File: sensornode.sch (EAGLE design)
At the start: 71 parts, among them IC1 CP2104, Q1 mmbt2222, Q2 mmbt2222, Q3 DMG3415U, SW2 KMR2, U1 TSL2591, U2 AP2112-3.3, U3 MCP73831T-2ACI/OT, U4 BMEx80, X2 ESP32_WROOM32_SKINNY, X4 20329

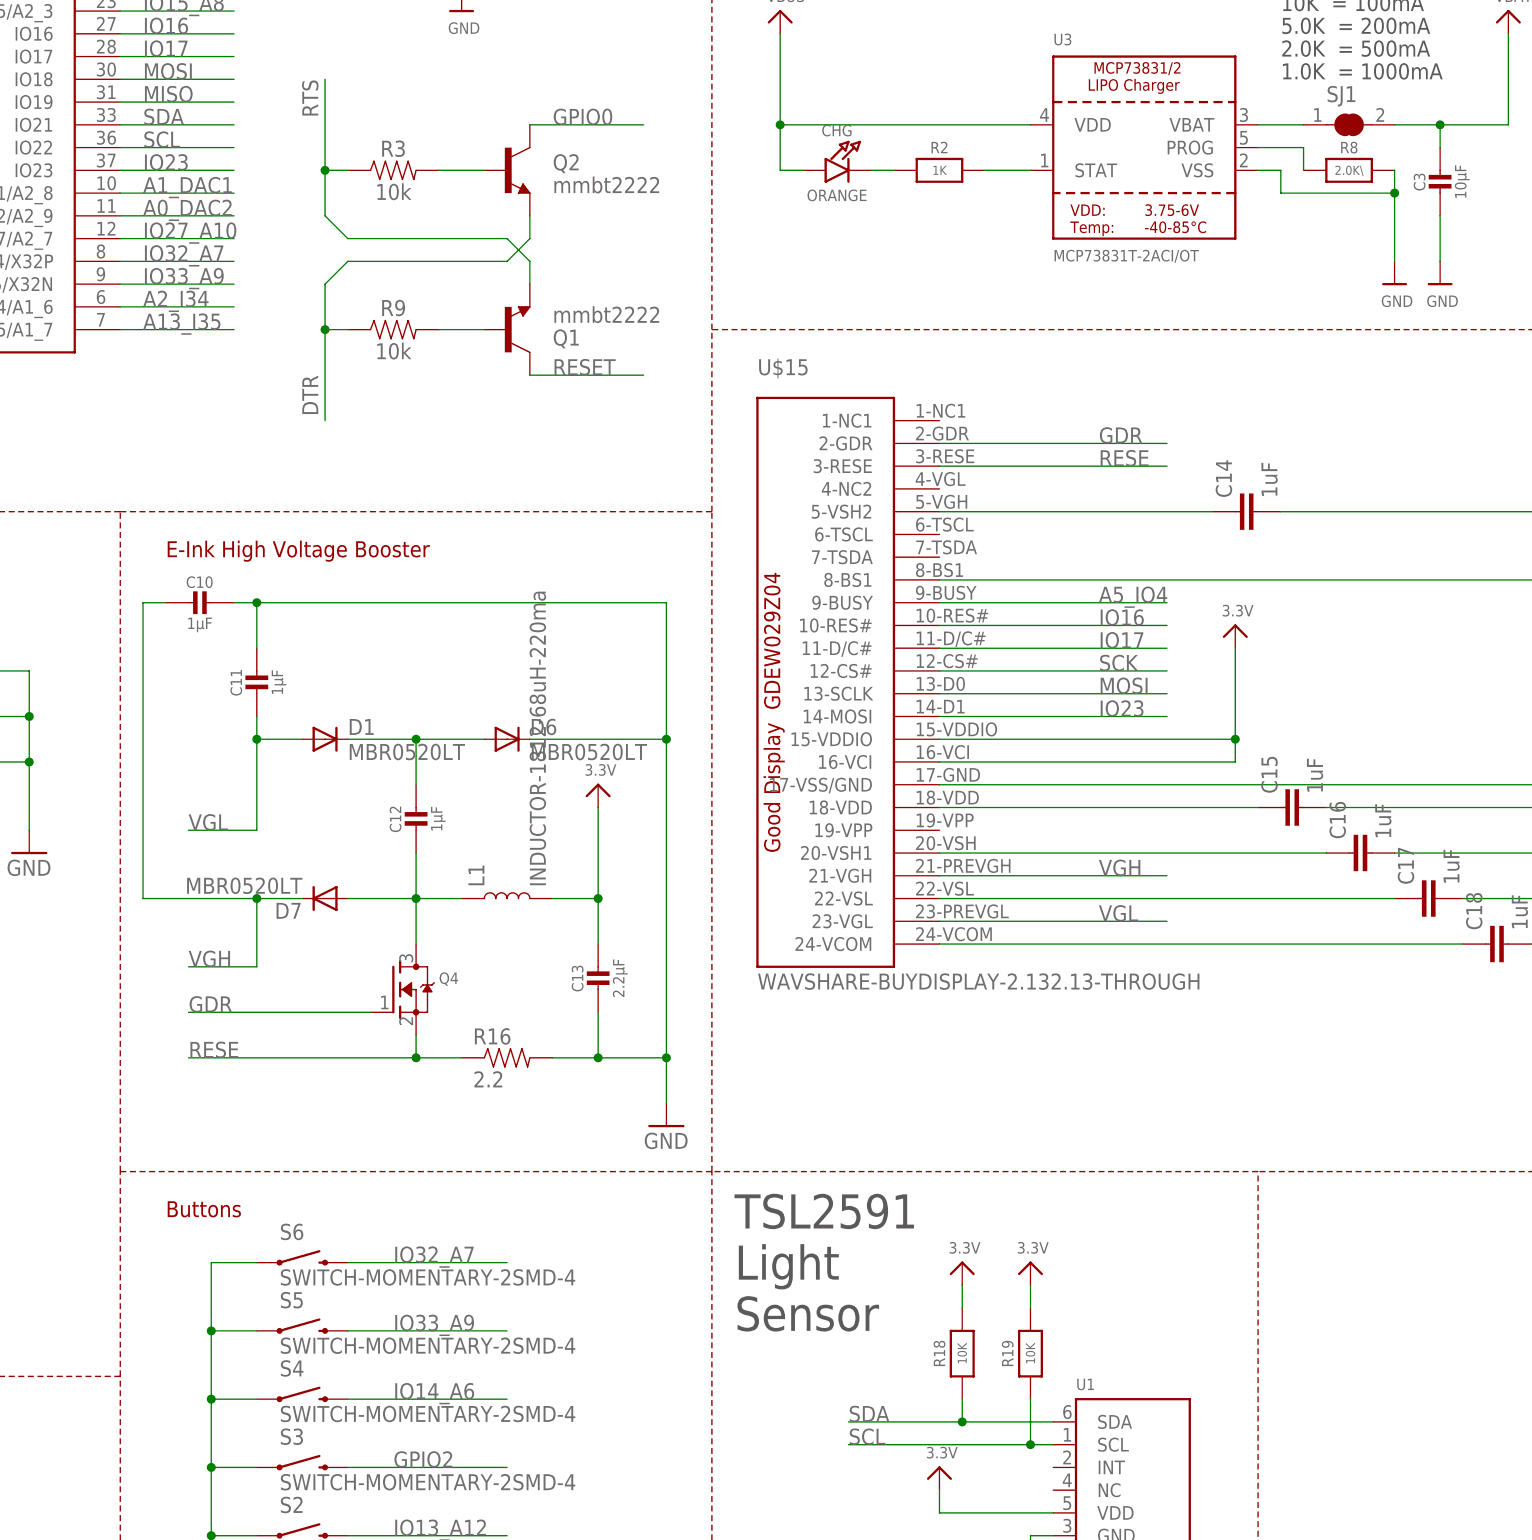
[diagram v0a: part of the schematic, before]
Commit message: Adjusting parts based on BOM generation
So there were a bunch of duplicated 0603 and 0805 parts, unifying
things to 0603s
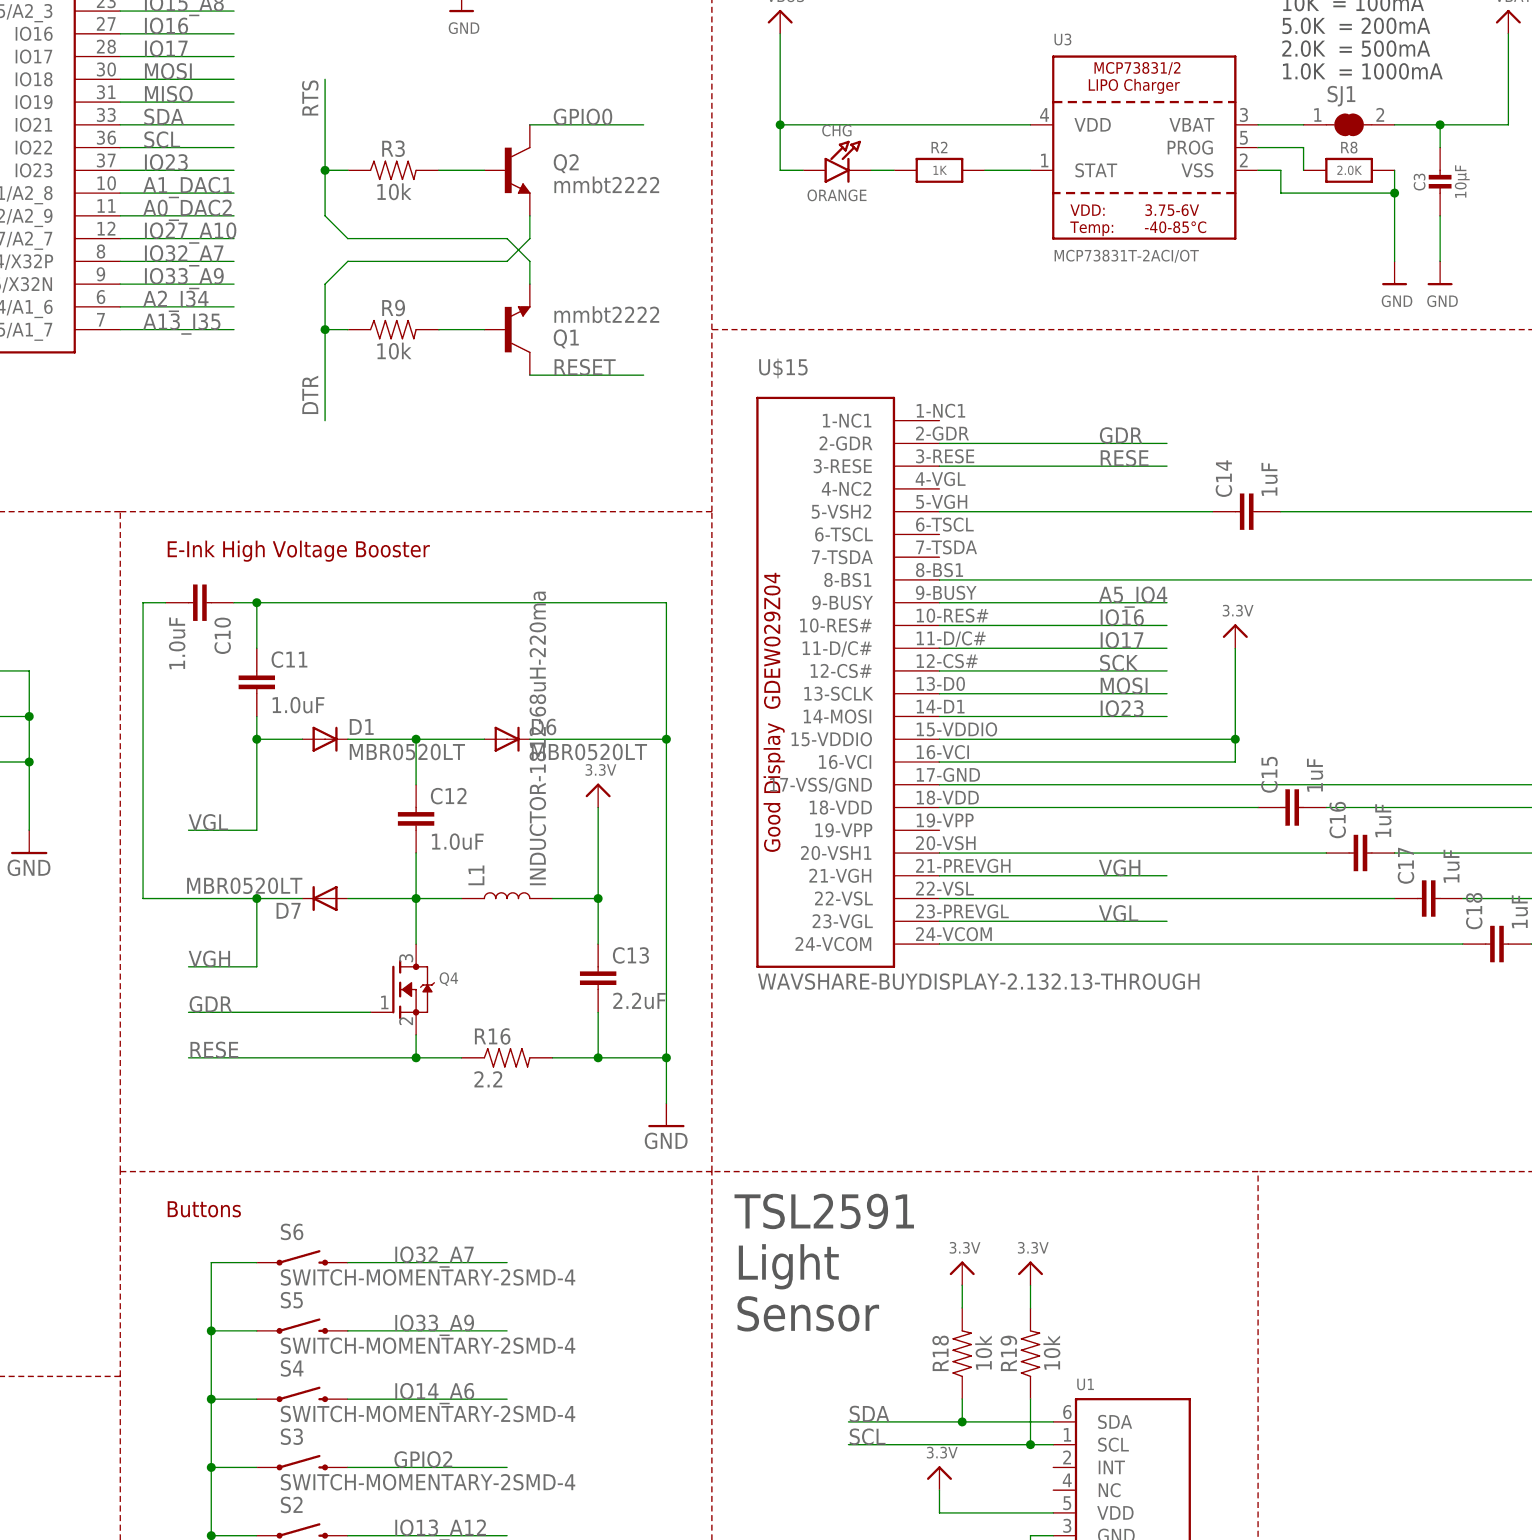
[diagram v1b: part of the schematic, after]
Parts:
- C10, C11, C12: value 1µF -> 1.0uF; device microbuilder:CAP_CERAMIC0805-NOOUTLINE -> SparkFun-Capacitors:1.0UF-0603-16V-10%
- C13: value 2.2µF -> 2.2uF; device microbuilder:CAP_CERAMIC0805-NOOUTLINE -> SparkFun-Capacitors:2.2UF-0603-10V-20%
- R18, R19: value 10K -> 10k; device microbuilder:RESISTOR0805_NOOUTLINE -> SparkFun-Resistors:10KOHM-0603-1/10W-1%
- R8: value 2.0K\ -> 2.0K
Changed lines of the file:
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@@
 <part name="C3" library="microbuilder" deviceset="CAP_CERAMIC" device="0805-NOOUTLINE" value="10µF"/>
 <part name="U$33" library="microbuilder" deviceset="GND" device=""/>
-<part name="R8" library="microbuilder" deviceset="RESISTOR" device="_0603_NOOUT" value="2.0K\"/>
+<part name="R8" library="microbuilder" deviceset="RESISTOR" device="_0603_NOOUT" value="2.0K"/>
 <part name="U$36" library="microbuilder" deviceset="GND" device=""/>
 <part name="U$38" library="microbuilder" deviceset="VBUS" device=""/>
@@
 <part name="SUPPLY5" library="SparkFun-Aesthetics" deviceset="3.3V" device=""/>
 <part name="GND10" library="SparkFun-Aesthetics" deviceset="GND" device=""/>
-<part name="C10" library="microbuilder" deviceset="CAP_CERAMIC" device="0805-NOOUTLINE" value="1µF"/>
-<part name="C11" library="microbuilder" deviceset="CAP_CERAMIC" device="0805-NOOUTLINE" value="1µF"/>
+<part name="C10" library="SparkFun-Capacitors" deviceset="1.0UF" device="-0603-16V-10%" value="1.0uF"/>
+<part name="C11" library="SparkFun-Capacitors" deviceset="1.0UF" device="-0603-16V-10%" value="1.0uF"/>
 <part name="GND2" library="SparkFun-Aesthetics" deviceset="GND" device=""/>
 <part name="D1" library="diode" deviceset="MBR0520LT" device=""/>
 <part name="D6" library="diode" deviceset="MBR0520LT" device=""/>
-<part name="C12" library="microbuilder" deviceset="CAP_CERAMIC" device="0805-NOOUTLINE" value="1µF"/>
+<part name="C12" library="SparkFun-Capacitors" deviceset="1.0UF" device="-0603-16V-10%" value="1.0uF"/>
 <part name="D7" library="diode" deviceset="MBR0520LT" device=""/>
 <part name="L1" library="SparkFun-Coils" deviceset="INDUCTOR" device="-1812" value="INDUCTOR-1812-68uH-220ma"/>
 <part name="U$2" library="microbuilder" deviceset="3.3V" device=""/>
-<part name="C13" library="microbuilder" deviceset="CAP_CERAMIC" device="0805-NOOUTLINE" value="2.2µF"/>
+<part name="C13" library="SparkFun-Capacitors" deviceset="2.2UF" device="-0603-10V-20%" value="2.2uF"/>
 <part name="Q4" library="adafruit" deviceset="MOSFET-N" device="REFLOW"/>
 <part name="R16" library="SparkFun-Resistors" deviceset="4.7KOHM-1/10W-1%(0603)" device="" value="2.2"/>
@@
 <part name="U$23" library="microbuilder" deviceset="3.3V" device=""/>
 <part name="U$27" library="microbuilder" deviceset="3.3V" device=""/>
-<part name="R18" library="microbuilder" deviceset="RESISTOR" device="0805_NOOUTLINE" value="10K"/>
-<part name="R19" library="microbuilder" deviceset="RESISTOR" device="0805_NOOUTLINE" value="10K"/>
+<part name="R18" library="SparkFun-Resistors" deviceset="10KOHM" device="-0603-1/10W-1%" value="10k"/>
+<part name="R19" library="SparkFun-Resistors" deviceset="10KOHM" device="-0603-1/10W-1%" value="10k"/>
 <part name="U$34" library="microbuilder" deviceset="3.3V" device=""/>
 <part name="U$43" library="microbuilder" deviceset="GND" device=""/>

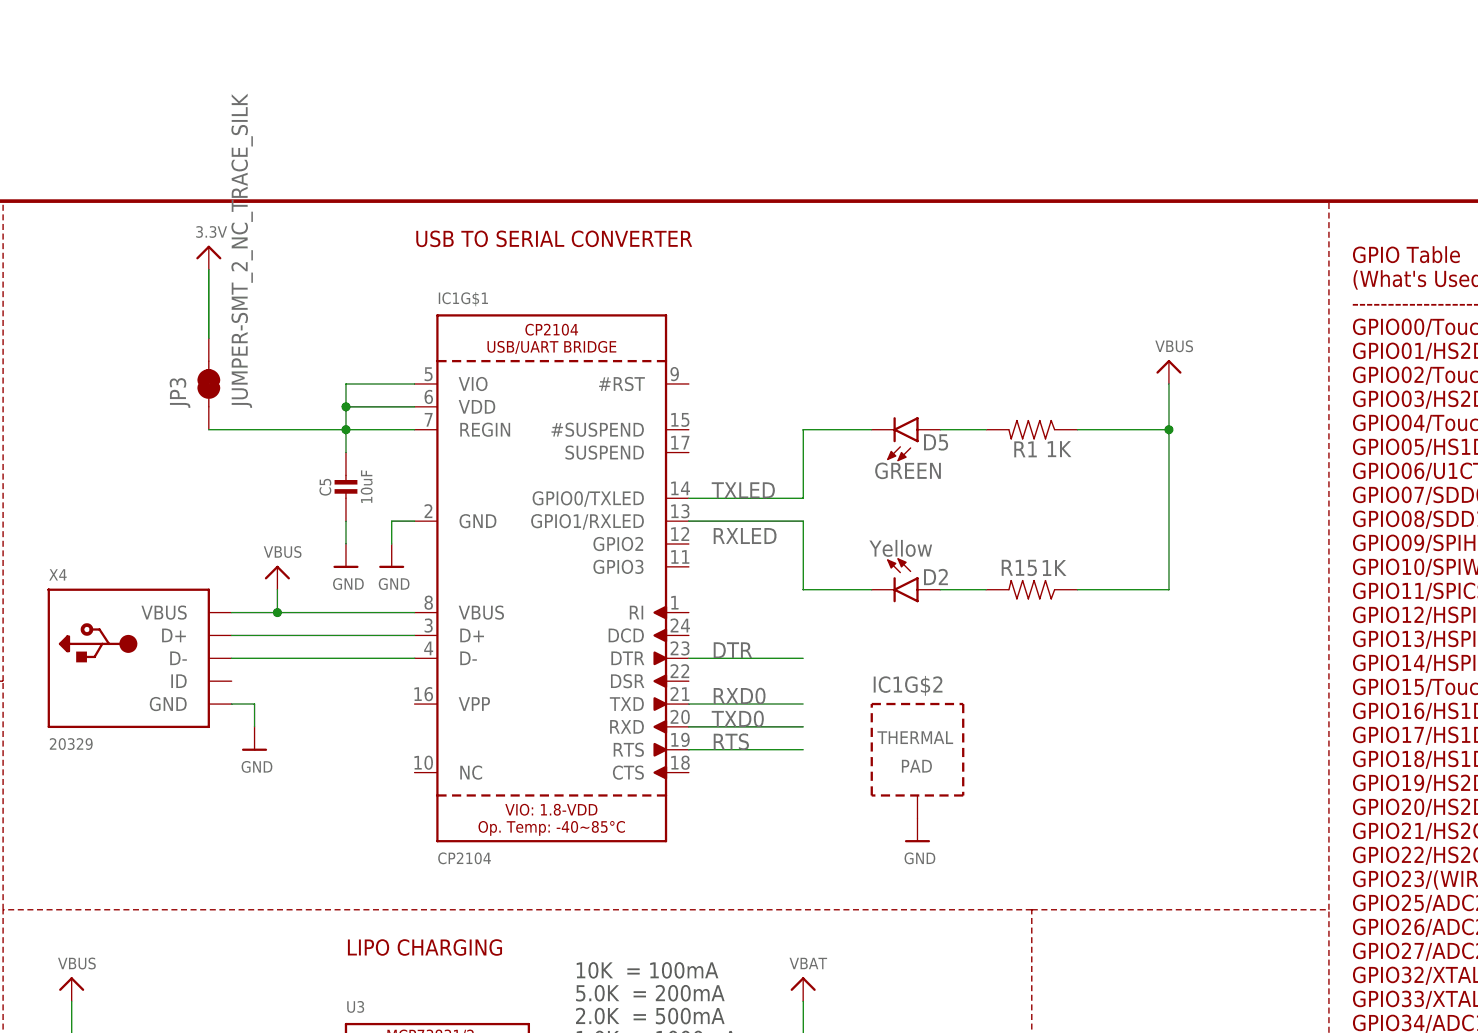
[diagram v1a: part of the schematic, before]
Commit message: USB-UART: switch to "USB Powered"
This changes the USB chip from being powered via the
regulated 3.3V line off the board, to being powered
via the USB VBUS power.  This should basically disable
the chip when the USB isn't plugged in.
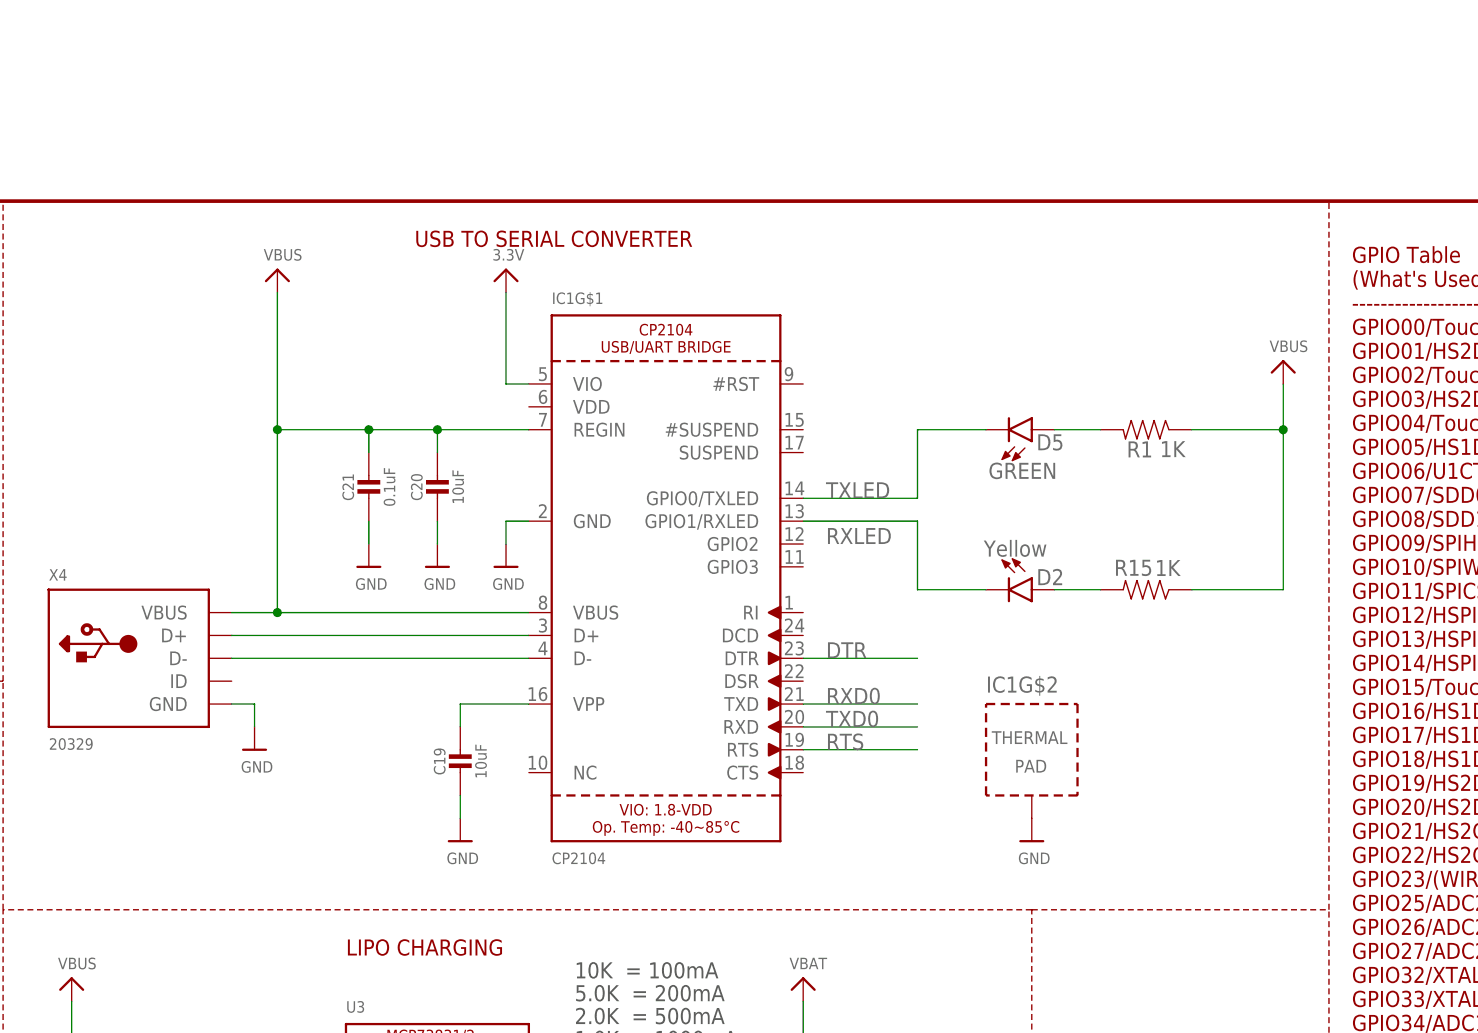
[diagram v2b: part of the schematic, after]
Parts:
- removed C5: 10uF, microbuilder:CAP_CERAMIC0805-NOOUTLINE
- removed JP3: JUMPER-SMT_2_NC_TRACE_SILK, SparkFun-Jumpers:JUMPER-SMT_2_NC_TRACE_SILK
- added C19, C20: 10uF, microbuilder:CAP_CERAMIC0805-NOOUTLINE
- added C21: 0.1uF, microbuilder:CAP_CERAMIC0805-NOOUTLINE
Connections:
- removed net N$6: C5.1, IC1G$1.REGIN, IC1G$1.VDD, IC1G$1.VIO, JP3.1
- new net N$23: C19.1, IC1G$1.VPP
- net 3.3V: now also IC1G$1.VIO; no longer JP3.2
- net GND: now also C19.2, C20.2, C21.2; no longer C5.2
- net VBUS: now also C20.1, C21.1, IC1G$1.REGIN
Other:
- moved on the sheet: D2, D5, IC1G$1, IC1G$2, R1, R15

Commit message: USB: Swapping the USB part out - twas unobtanium
the 4UCONN connector that Adafruit used is basically made of unobtanium
and more or less doesn't exist.  The part that was trying to be used
the rear prongs did not match up by any stretch of the imagination.

A mess of e-mails an annoyance ensued.

I'm swapping out the part on everything I can now, this seems to be
more common, and there's parts that are similar enough to it that
replacing it won't be a big deal.  New part is the
Amphenol FCI 10118193-0001LF
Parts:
- X4: device microbuilder:USB_MICRO_20329_V2 -> microbuilder:MICRO-USB-SMD-B-(10118193-0001LF)-ADASYM
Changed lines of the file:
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@@
 <layer number="115" name="ReferenceISLANDS" color="7" fill="1" visible="yes" active="yes"/>
 <layer number="116" name="Patch_BOT" color="9" fill="4" visible="yes" active="yes"/>
+<layer number="117" name="BACKMAAT1" color="7" fill="1" visible="no" active="no"/>
 <layer number="118" name="Rect_Pads" color="7" fill="1" visible="yes" active="yes"/>
+<layer number="119" name="KAP_TEKEN" color="7" fill="1" visible="no" active="no"/>
+<layer number="120" name="KAP_MAAT1" color="7" fill="1" visible="no" active="no"/>
 <layer number="121" name="_tsilk" color="7" fill="1" visible="yes" active="yes"/>
 <layer number="122" name="_bsilk" color="7" fill="1" visible="yes" active="yes"/>
@@
 <layer number="128" name="_bValues" color="7" fill="1" visible="yes" active="yes"/>
 <layer number="129" name="Mask" color="7" fill="1" visible="yes" active="yes"/>
+<layer number="130" name="SMDSTROOK" color="7" fill="1" visible="no" active="no"/>
 <layer number="131" name="tAdjust" color="7" fill="1" visible="yes" active="yes"/>
 <layer number="132" name="bAdjust" color="7" fill="1" visible="yes" active="yes"/>
+<layer number="133" name="bottom_silk" color="7" fill="1" visible="no" active="no"/>
 <layer number="144" name="Drill_legend" color="7" fill="1" visible="yes" active="yes"/>
 <layer number="145" name="DrillLegend_01-16" color="2" fill="9" visible="no" active="yes"/>
@@
 <part name="R10" library="microbuilder" deviceset="RESISTOR" device="_0603_NOOUT" value="1K"/>
 <part name="IC1" library="microbuilder" deviceset="CP2104" device="" value="CP2104"/>
-<part name="X4" library="microbuilder" deviceset="USB" device="_MICRO_20329_V2" value="20329"/>
+<part name="X4" library="microbuilder" deviceset="MICRO-USB-SMD-B-(10118193-0001LF)-ADASYM" device="" value="20329"/>
 <part name="U$11" library="microbuilder" deviceset="GND" device=""/>
 <part name="U$12" library="microbuilder" deviceset="GND" device=""/>
